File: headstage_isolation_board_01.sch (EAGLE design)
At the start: 15 parts

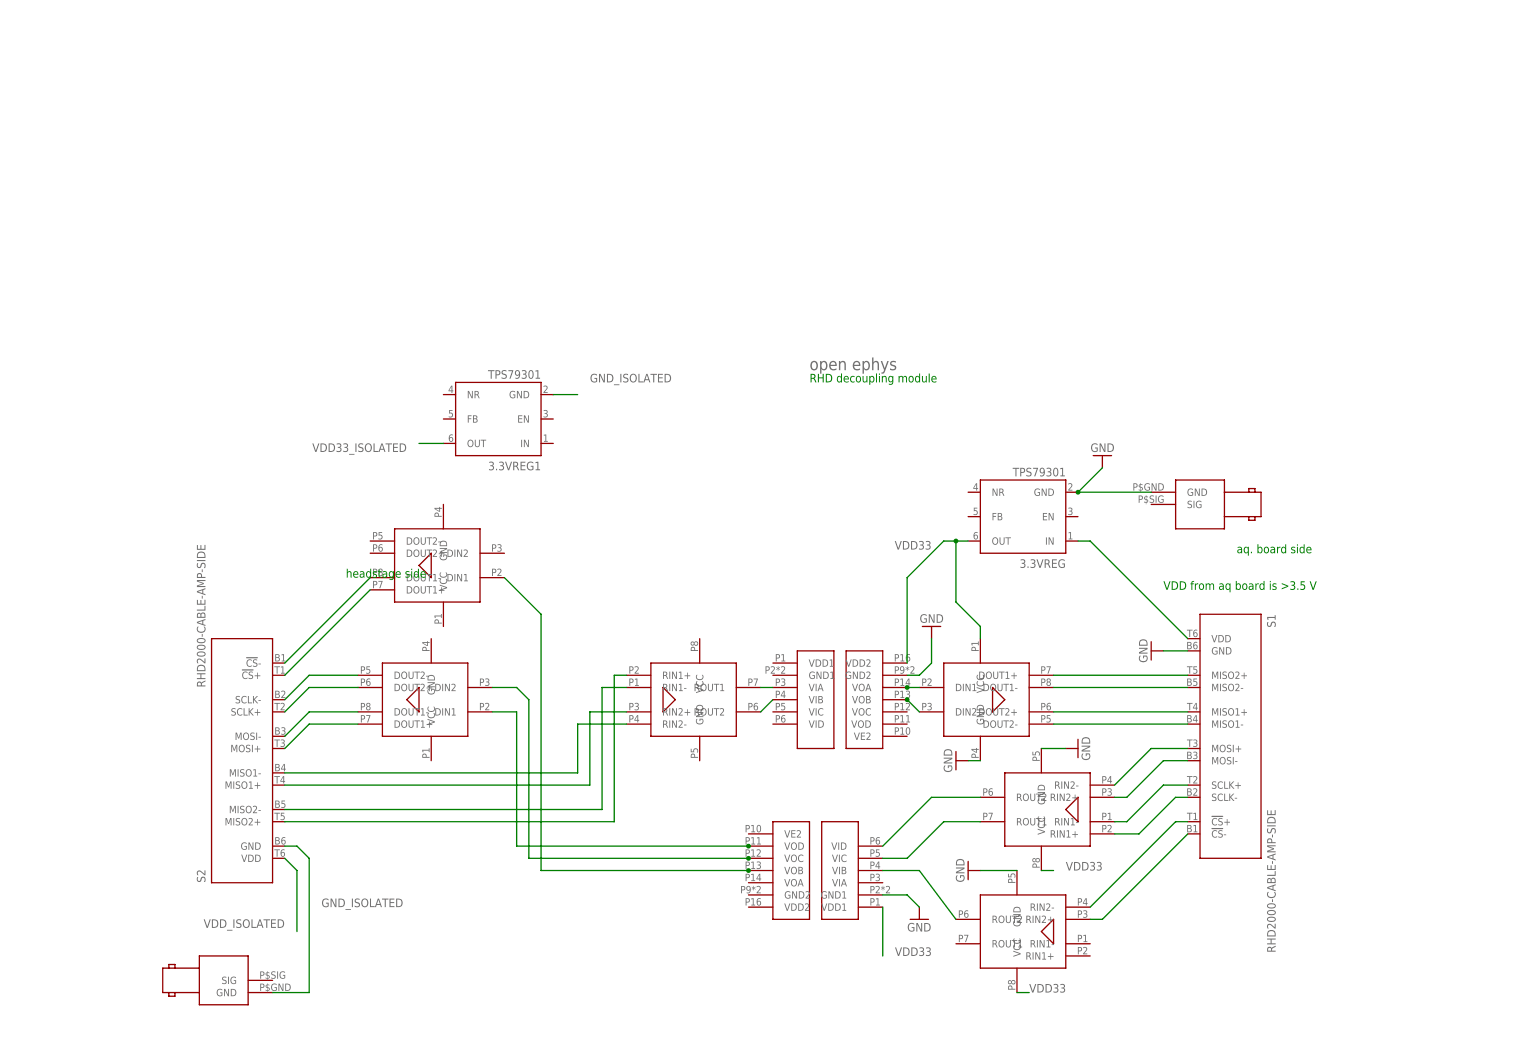
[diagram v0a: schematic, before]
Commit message: added DC-DC converter
still missing resistors etc
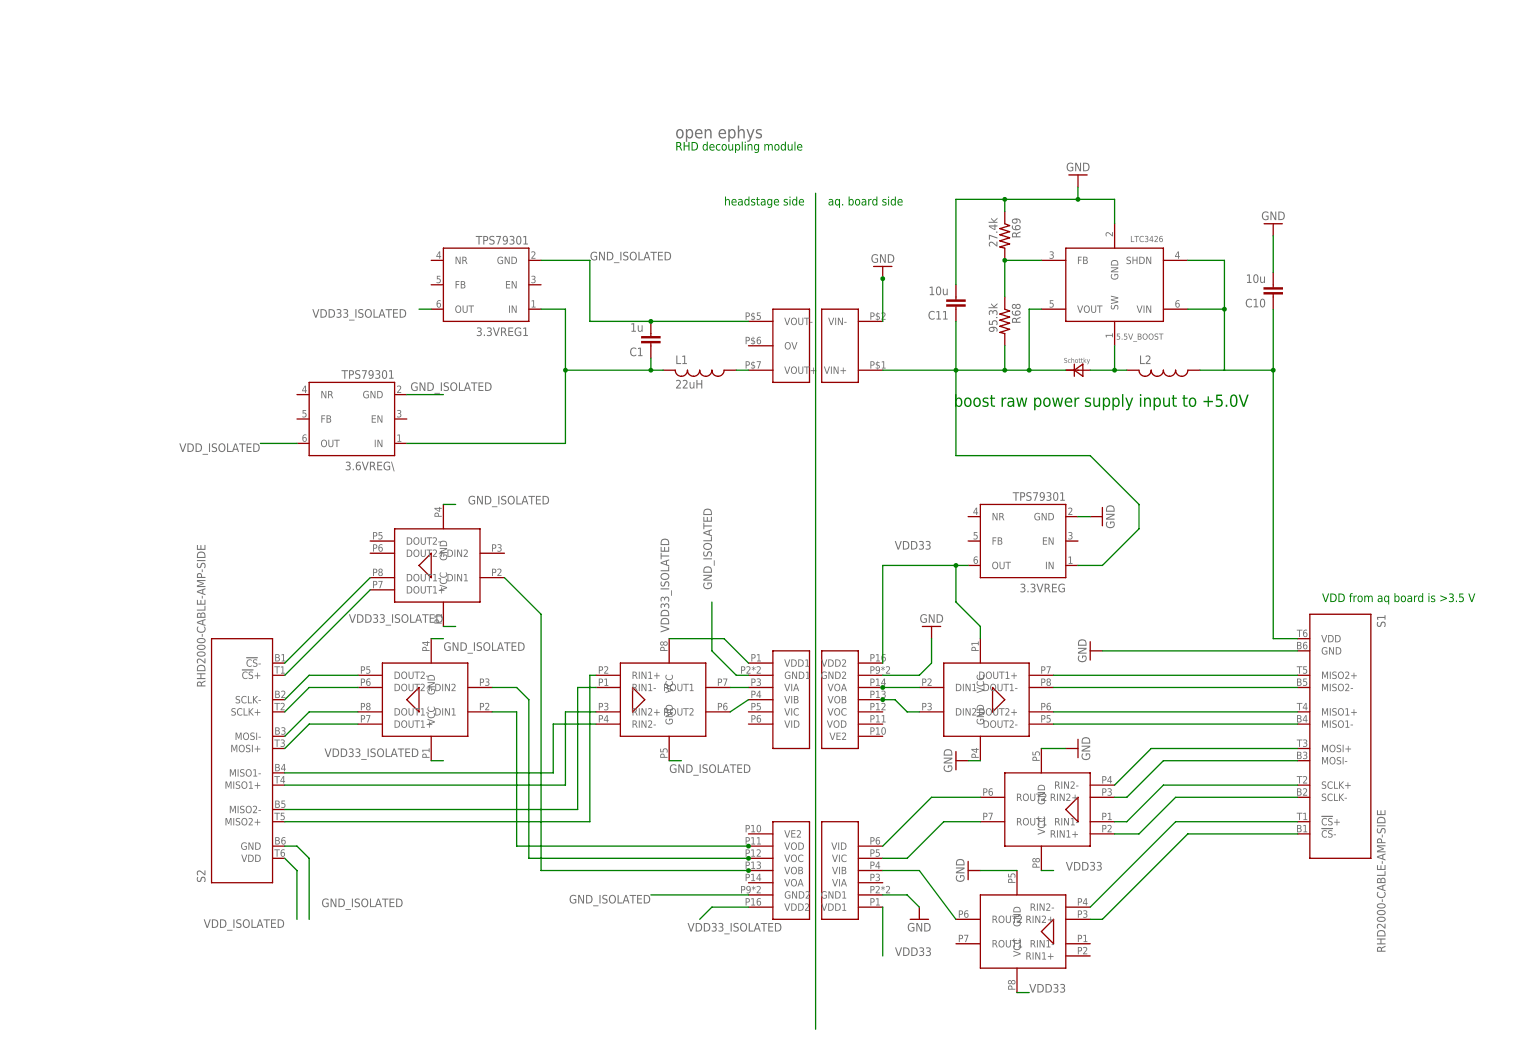
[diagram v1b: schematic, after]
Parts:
- removed U$11, U$3: BNC_RIGHT_ANGLE, open-ephys_old:BNC_RIGHT_ANGLE
- added 3.6VREG\: TPS79301, RHD2000_eval_board:TPS79301
- added 5.5V_BOOST: LTC3426, open-ephys:LTC3426
- added C1: 1u, RHD2000_eval_board:C_1206
- added C10, C11: 10u, RHD2000_eval_board:C_1206
- added D1: MBRA210LT3-D, open-ephys:MBRA210LT3-D
- added L1: 22uH, RHD2000_eval_board:L_1206
- added L2: (no value), RHD2000_eval_board:L_1206
- added R68: 95.3k, RHD2000_eval_board:R_0603
- added R69: 27.4k, RHD2000_eval_board:R_0603
- added U$12: NMV0505, open-ephys:NMV0505
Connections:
- removed net N$31: 3.3VREG.IN, S1.VDD
- new net 5VBOOST: 3.3VREG.IN, 5.5V_BOOST.VOUT, C11.1, D1.NEG, R68.2, U$12.VIN+
- new net N$276: 5.5V_BOOST.FB, R68.1, R69.2
- new net N$278: 5.5V_BOOST.SW, D1.POS, L2.2
- new net N$32: L1.1, U$12.VOUT+
- new net N$34: 3.3VREG1.IN, 3.6VREG\.IN, C1.1, L1.2
- new net VDD_IN: 5.5V_BOOST.SHDN, 5.5V_BOOST.VIN, C10.1, L2.1, S1.VDD
- net GND: now also 5.5V_BOOST.GND, C10.2, C11.2, R69.1, U$12.VIN-; no longer U$11.GND
- net GND_ISOLATED: now also 3.6VREG\.GND, C1.2, U$10.GND1, U$12.VOUT-, U$2.GND2, U$5.GND, U$6.GND, U$9.GND; no longer U$3.GND
- net VDD33_ISOLATED: now also U$10.VDD1, U$2.VDD2, U$5.VCC, U$6.VCC, U$9.VCC
- net VDD_ISOLATED: now also 3.6VREG\.OUT
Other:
- note added: "boost raw power supply input to +5.0V"
- moved on the sheet: 3.3VREG, 3.3VREG1, S1

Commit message: initial partial layout, added some regulator parts
still need to change r values for regulators
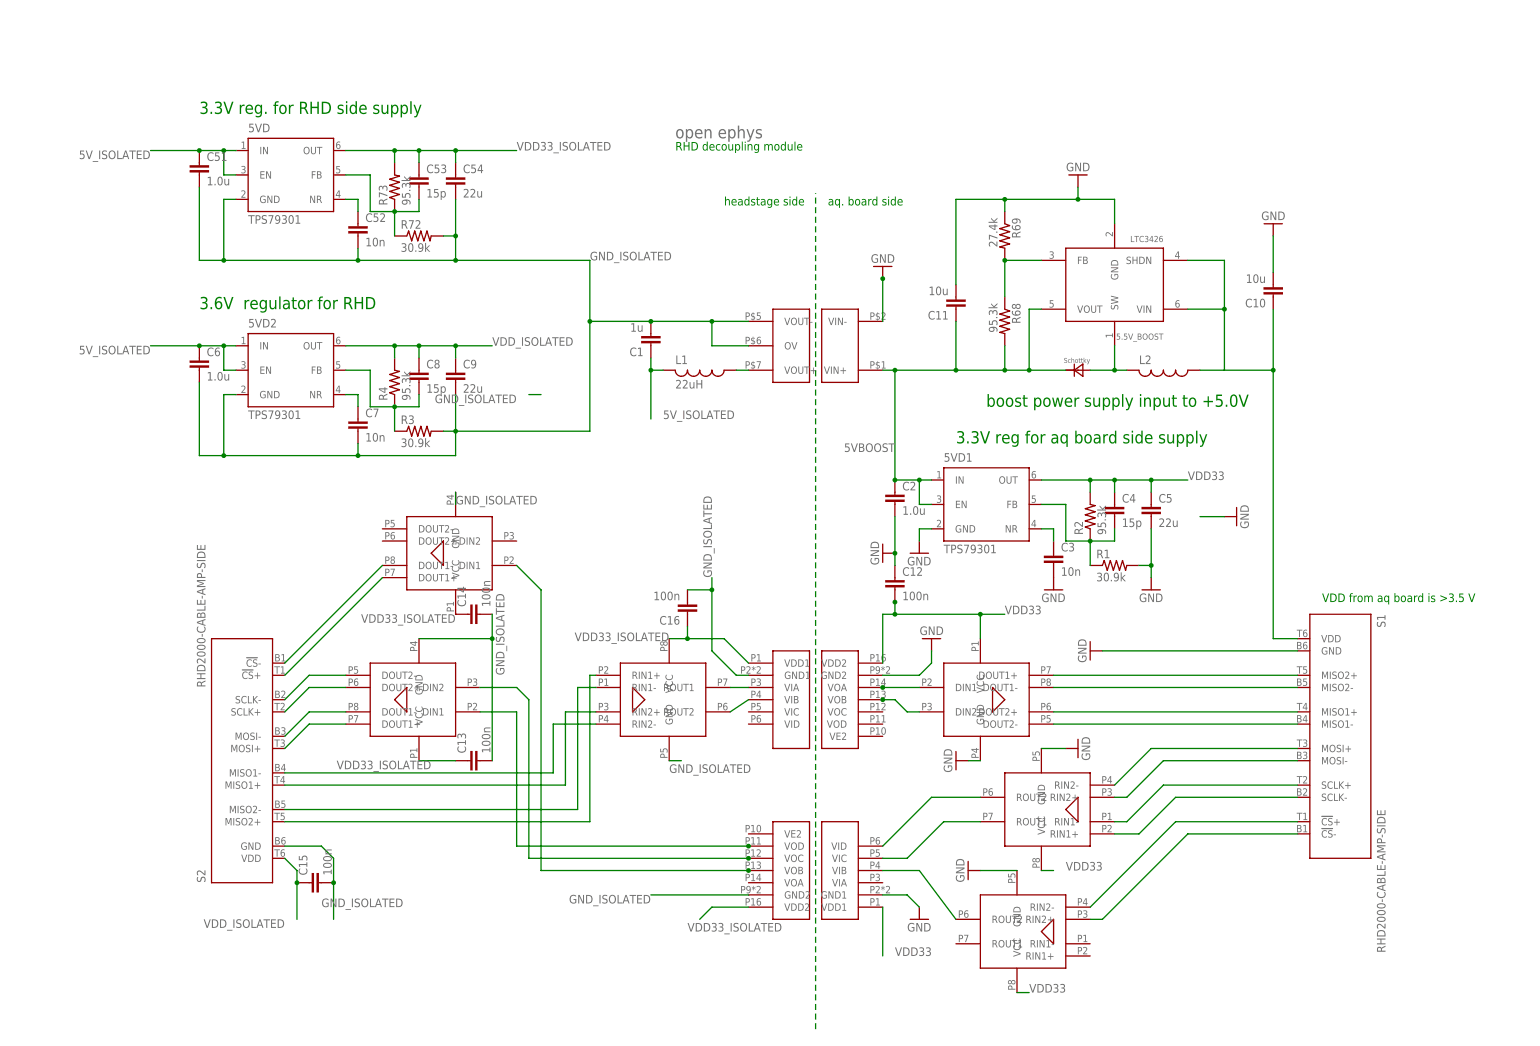
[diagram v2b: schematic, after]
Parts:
- removed 3.3VREG, 3.3VREG1, 3.6VREG\: TPS79301, RHD2000_eval_board:TPS79301
- added 5VD, 5VD1, 5VD2: TPS79301, RHD2000_eval_board:TPS79301
- added C12, C13, C14, C15, C16: 100n, RHD2000_eval_board:C_0603
- added C2, C51, C6: 1.0u, RHD2000_eval_board:C_0805
- added C3, C52, C7: 10n, RHD2000_eval_board:C_0603
- added C4, C53, C8: 15p, RHD2000_eval_board:C_0603
- added C5, C54, C9: 22u, RHD2000_eval_board:C_1206
- added R1, R3, R72: 30.9k, RHD2000_eval_board:R_0603
- added R2, R4, R73: 95.3k, RHD2000_eval_board:R_0603
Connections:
- removed net N$34: 3.3VREG1.IN, 3.6VREG\.IN, C1.1, L1.2
- new net 5V_ISOLATED: 5VD.EN, 5VD.IN, 5VD2.EN, 5VD2.IN, C1.1, C51.1, C6.1, L1.2
- new net GND4: C15.2
- new net N$108: 5VD.FB, C53.2, R72.1, R73.1
- new net N$33: 5VD1.NR, C3.1
- new net N$35: 5VD1.FB, C4.2, R1.1, R2.1
- new net N$36: 5VD2.NR, C7.1
- new net N$37: 5VD2.FB, C8.2, R3.1, R4.1
- new net N$97: 5VD.NR, C52.1
- net 5VBOOST: now also 5VD1.EN, 5VD1.IN, C2.1; no longer 3.3VREG.IN
- net GND: now also 5VD1.GND, C12.1, C2.2, C3.2, C5.2, R1.2; no longer 3.3VREG.GND
- net GND_ISOLATED: now also 5VD.GND, 5VD2.GND, C13.2, C14.2, C16.2, C51.2, C52.2, C54.2, C6.2, C7.2, C9.2, R3.2, R72.2, U$12.OV; no longer 3.3VREG1.GND, 3.6VREG\.GND
- net VDD33: now also 5VD1.OUT, C12.2, C4.1, C5.1, R2.2; no longer 3.3VREG.OUT
- net VDD33_ISOLATED: now also 5VD.OUT, C13.1, C14.1, C16.1, C53.1, C54.1, R73.2; no longer 3.3VREG1.OUT
- net VDD_ISOLATED: now also 5VD2.OUT, C15.1, C8.1, C9.1, R4.2; no longer 3.6VREG\.OUT
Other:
- note added: "3.3V reg for aq board side supply"
- note added: "3.3V reg. for RHD side supply"
- note added: "3.6V regulator for RHD"
- note added: "boost power supply input to +5.0V"
- note removed: "boost raw power supply input to +5.0V"

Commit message: initial rough layout
still missing correct resistor values
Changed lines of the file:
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@@
 <text x="64.77" y="52.07" size="1.778" layer="91">aq. board side</text>
 <text x="167.64" y="-30.48" size="1.778" layer="91">VDD from aq board is &gt;3.5 V</text>
-<text x="33.02" y="63.5" size="1.778" layer="91">RHD decoupling module</text>
+<text x="60.96" y="58.42" size="1.778" layer="91">RHD decoupling module</text>
 <text x="152.4" y="12.7" size="2.54" layer="91" rot="R180">boost power supply input to +5.0V</text>
 <text x="-66.04" y="71.12" size="2.54" layer="91">3.3V reg. for RHD side supply</text>
@@
 <instance part="GND6" gate="1" x="91.44" y="-63.5" rot="R270"/>
 <instance part="S1" gate="A" x="170.18" y="-58.42" rot="R90"/>
-<instance part="U$1" gate="G$1" x="33.02" y="66.04"/>
+<instance part="U$1" gate="G$1" x="60.96" y="60.96"/>
 <instance part="U$4" gate="G$1" x="101.6" y="-55.88"/>
 <instance part="U$6" gate="G$1" x="34.29" y="-53.34"/>
@@
 <pinref part="S2" gate="A" pin="GND"/>
 <wire x1="-40.64" y1="-81.28" x2="-48.26" y2="-81.28" width="0.1524" layer="91"/>
-<label x="-40.64" y="-93.98" size="1.778" layer="95"/>
+<label x="-38.1" y="-96.52" size="1.778" layer="95"/>
 <wire x1="-38.1" y1="-83.82" x2="-38.1" y2="-96.52" width="0.1524" layer="91"/>
 </segment>

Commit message: routing cleanup, added more bypass caps
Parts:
- added C17, C18: 100n, RHD2000_eval_board:C_0603
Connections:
- net GND: now also C17.1, C18.2
- net VDD33: now also C17.2, C18.1, U$10.VE2
- net VDD33_ISOLATED: now also U$2.VE2
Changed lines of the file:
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@@
 <part name="C15" library="RHD2000_eval_board" deviceset="C" device="_0603" value="100n"/>
 <part name="C16" library="RHD2000_eval_board" deviceset="C" device="_0603" value="100n"/>
+<part name="C17" library="RHD2000_eval_board" deviceset="C" device="_0603" value="100n"/>
+<part name="C18" library="RHD2000_eval_board" deviceset="C" device="_0603" value="100n"/>
 </parts>
 <sheets>
@@
 <instance part="U$2" gate="G$1" x="60.96" y="-83.82" rot="R180"/>
 <instance part="GND4" gate="1" x="83.82" y="-96.52"/>
-<instance part="GND5" gate="1" x="119.38" y="-40.64" rot="R270"/>
+<instance part="GND5" gate="1" x="121.92" y="-33.02" rot="R180"/>
 <instance part="GND7" gate="1" x="149.86" y="-12.7" rot="R90"/>
 <instance part="GND95" gate="1" x="76.2" y="39.37" rot="R180"/>
@@
 <instance part="C15" gate="C" x="-43.18" y="-88.9" rot="R90"/>
 <instance part="C16" gate="C" x="35.56" y="-33.02" rot="R180"/>
+<instance part="C17" gate="C" x="78.74" y="-93.98"/>
+<instance part="C18" gate="C" x="99.06" y="-38.1" rot="R90"/>
 </instances>
 <busses>
@@
 <segment>
 <pinref part="U$2" gate="G$1" pin="GND1"/>
-<wire x1="76.2" y1="-91.44" x2="81.28" y2="-91.44" width="0.1524" layer="91"/>
+<wire x1="76.2" y1="-91.44" x2="78.74" y2="-91.44" width="0.1524" layer="91"/>
 <pinref part="GND4" gate="1" pin="GND"/>
+<wire x1="78.74" y1="-91.44" x2="81.28" y2="-91.44" width="0.1524" layer="91"/>
 <wire x1="81.28" y1="-91.44" x2="83.82" y2="-93.98" width="0.1524" layer="91"/>
+<pinref part="C17" gate="C" pin="1"/>
+<junction x="78.74" y="-91.44"/>
 </segment>
 <segment>
 <pinref part="S1" gate="A" pin="GND"/>
 <pinref part="GND5" gate="1" pin="GND"/>
+<wire x1="121.92" y1="-35.56" x2="121.92" y2="-38.1" width="0.1524" layer="91"/>
+<wire x1="121.92" y1="-38.1" x2="121.92" y2="-40.64" width="0.1524" layer="91"/>
 <wire x1="121.92" y1="-40.64" x2="162.56" y2="-40.64" width="0.1524" layer="91"/>
+<pinref part="C18" gate="C" pin="2"/>
+<wire x1="104.14" y1="-38.1" x2="121.92" y2="-38.1" width="0.1524" layer="91"/>
+<junction x="121.92" y="-38.1"/>
 </segment>
 <segment>
@@
 <segment>
 <pinref part="U$2" gate="G$1" pin="VDD1"/>
-<wire x1="76.2" y1="-93.98" x2="76.2" y2="-104.14" width="0.1524" layer="91"/>
+<wire x1="76.2" y1="-93.98" x2="76.2" y2="-99.06" width="0.1524" layer="91"/>
 <label x="78.74" y="-104.14" size="1.778" layer="95"/>
+<pinref part="C17" gate="C" pin="2"/>
+<wire x1="76.2" y1="-99.06" x2="76.2" y2="-111.76" width="0.1524" layer="91"/>
+<wire x1="78.74" y1="-99.06" x2="76.2" y2="-99.06" width="0.1524" layer="91"/>
+<junction x="76.2" y="-99.06"/>
 </segment>
 <segment>
@@
 <wire x1="78.74" y1="-30.48" x2="78.74" y2="-33.02" width="0.1524" layer="91"/>
 <junction x="78.74" y="-33.02"/>
+<pinref part="C18" gate="C" pin="1"/>
+<junction x="96.52" y="-38.1"/>
+</segment>
+<segment>
+<pinref part="U$10" gate="G$1" pin="VE2"/>
+<wire x1="76.2" y1="-58.42" x2="81.28" y2="-58.42" width="0.1524" layer="91"/>
+<wire x1="81.28" y1="-58.42" x2="81.28" y2="-60.96" width="0.1524" layer="91"/>
+<label x="81.28" y="-60.96" size="1.778" layer="95" rot="R270"/>
 </segment>
 </net>
@@
 <wire x1="40.64" y1="-93.98" x2="38.1" y2="-96.52" width="0.1524" layer="91"/>
 <label x="35.56" y="-99.06" size="1.778" layer="95"/>
-</segment>
-</net>
+<pinref part="U$2" gate="G$1" pin="VE2"/>
+<wire x1="48.26" y1="-78.74" x2="40.64" y2="-78.74" width="0.1524" layer="91"/>
+<wire x1="40.64" y1="-78.74" x2="40.64" y2="-93.98" width="0.1524" layer="91"/>
+<junction x="40.64" y="-93.98"/>
+</segment>
+</net>

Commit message: fix some naming CONNECTOR STILL WRONG- DONT USE YET
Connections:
- net N$1 renamed MISO2+
- net N$14 renamed SCLK-
- net N$15 renamed SCLK+
- net N$16 renamed MOSI-
- net N$17 renamed MOSI+
- net N$18 renamed CS-
- net N$19 renamed CS+
- net N$2 renamed MISO2-
- net N$3 renamed MISO1+
- net N$4 renamed MISO1-
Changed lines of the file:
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@@
 <?xml version="1.0" encoding="utf-8"?>
 <!DOCTYPE eagle SYSTEM "eagle.dtd">
-<eagle version="6.1">
+<eagle version="6.3">
 <drawing>
 <settings>
@@
 </busses>
 <nets>
-<net name="N$1" class="0">
+<net name="MISO2+" class="0">
 <segment>
 <pinref part="S1" gate="A" pin="MISO2+"/>
@@
 </segment>
 </net>
-<net name="N$2" class="0">
+<net name="MISO2-" class="0">
 <segment>
 <pinref part="S1" gate="A" pin="MISO2-"/>
@@
 </segment>
 </net>
-<net name="N$3" class="0">
+<net name="MISO1+" class="0">
 <segment>
 <pinref part="S1" gate="A" pin="MISO1+"/>
@@
 </segment>
 </net>
-<net name="N$4" class="0">
+<net name="MISO1-" class="0">
 <segment>
 <pinref part="S1" gate="A" pin="MISO1-"/>
@@
 </segment>
 </net>
-<net name="N$14" class="0">
+<net name="SCLK-" class="0">
 <segment>
 <pinref part="S1" gate="A" pin="SCLK-"/>
@@
 </segment>
 </net>
-<net name="N$15" class="0">
+<net name="SCLK+" class="0">
 <segment>
 <pinref part="S1" gate="A" pin="SCLK+"/>
@@
 </segment>
 </net>
-<net name="N$16" class="0">
+<net name="MOSI-" class="0">
 <segment>
 <pinref part="S1" gate="A" pin="MOSI-"/>
@@
 </segment>
 </net>
-<net name="N$17" class="0">
+<net name="MOSI+" class="0">
 <segment>
 <pinref part="S1" gate="A" pin="MOSI+"/>
@@
 </segment>
 </net>
-<net name="N$18" class="0">
+<net name="CS-" class="0">
 <segment>
 <pinref part="S1" gate="A" pin="!CS!-"/>
@@
 </segment>
 </net>
-<net name="N$19" class="0">
+<net name="CS+" class="0">
 <segment>
 <pinref part="S1" gate="A" pin="!CS!+"/>
